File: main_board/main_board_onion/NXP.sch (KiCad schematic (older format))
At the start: 16 parts

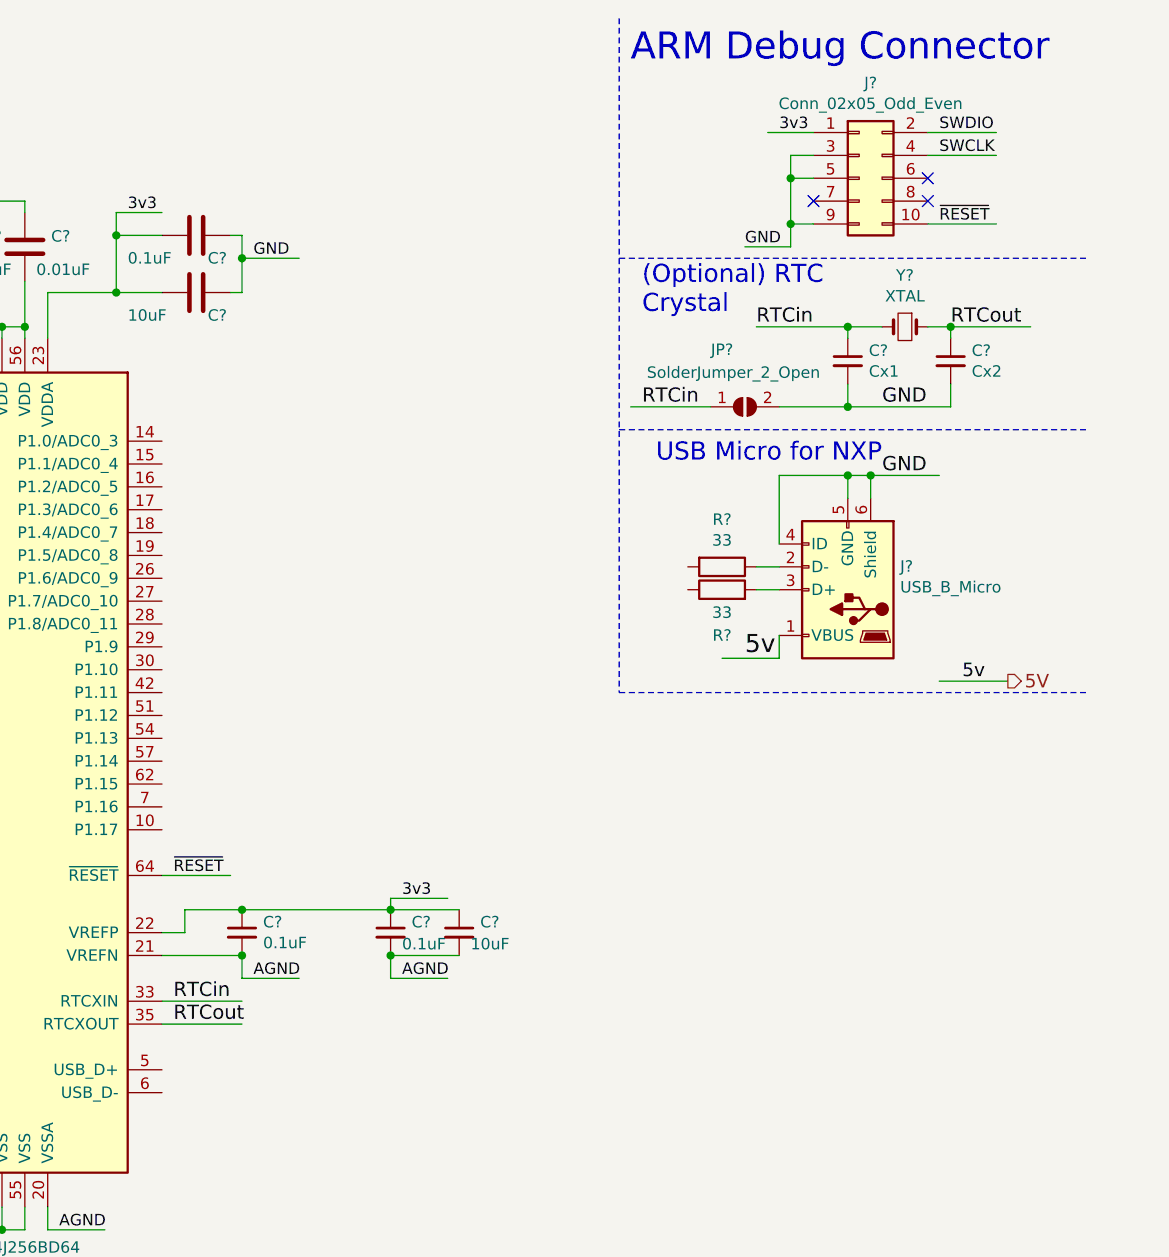
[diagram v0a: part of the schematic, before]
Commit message: Added USB support. Minor additions to Omega board.
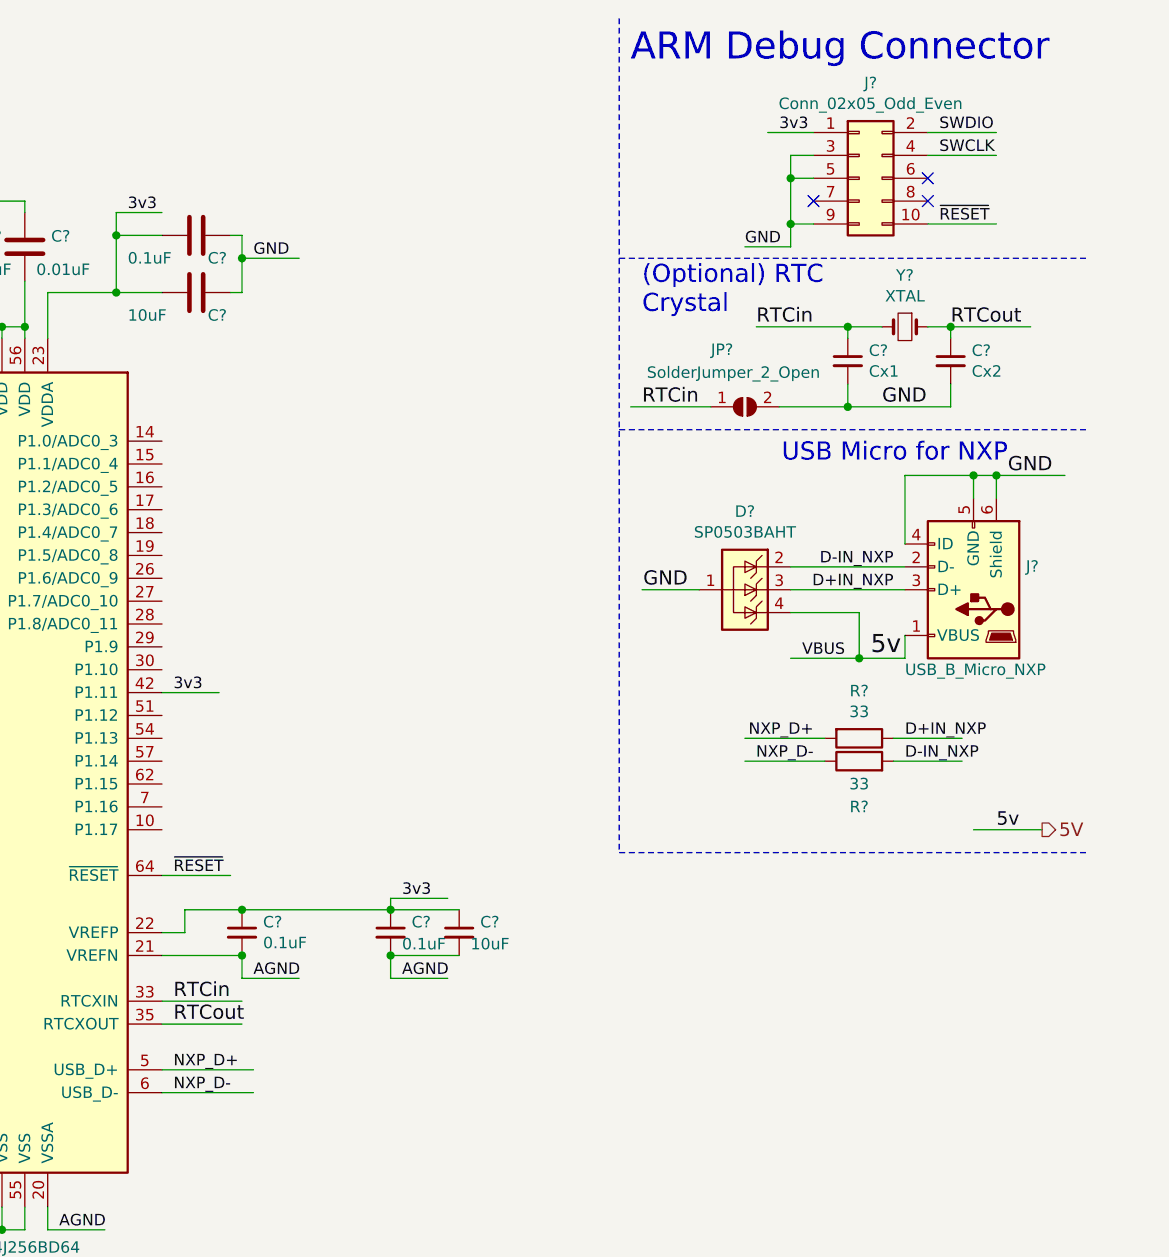
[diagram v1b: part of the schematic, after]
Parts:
- added D?: SP0503BAHT, Package_TO_SOT_SMD:SOT-143, symbol Power_Protection:SP0503BAHT
- J?: value USB_B_Micro -> USB_B_Micro_NXP; footprint (none) -> Connector_USB:USB_Micro-B_Molex-105017-0001
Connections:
- net labels added: D+IN_NXP, D-IN_NXP, NXP_D+, NXP_D-, VBUS
- wire segments 89 -> 100
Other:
- moved on the sheet: J?, R?
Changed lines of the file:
@@
 EESchema Schematic File Version 4
+LIBS:main_board_onion-cache
 EELAYER 26 0
 EELAYER END
 $Descr A4 11693 8268
 encoding utf-8
-Sheet 2 2
+Sheet 2 3
 Title ""
 Date ""
@@
 L Connector:USB_B_Micro J?
 U 1 1 5B63D16B
-P 10150 3000
-F 0 "J?" H 9921 2898 50  0000 R CNN
-F 1 "USB_B_Micro" H 9921 2989 50  0000 R CNN
-F 2 "" H 10300 2950 50  0001 C CNN
-F 3 "~" H 10300 2950 50  0001 C CNN
-	1    10150 3000
+P 10700 3000
+F 0 "J?" H 10471 2898 50  0000 R CNN
+F 1 "USB_B_Micro_NXP" H 11000 3350 50  0000 R CNN
+F 2 "Connector_USB:USB_Micro-B_Molex-105017-0001" H 10850 2950 50  0001 C CNN
+F 3 "~" H 10850 2950 50  0001 C CNN
+	1    10700 3000
 	-1   0    0    1
 $EndComp
 Wire Wire Line
-	10150 2600 10150 2500
-Wire Wire Line
-	10150 2500 10250 2500
-Wire Wire Line
-	10250 2600 10250 2500
-Connection ~ 10250 2500
-Wire Wire Line
-	10250 2500 10550 2500
-Text Label 10300 2500 0    62   ~ 0
-GND
-Wire Wire Line
-	9850 2800 9850 2500
-Wire Wire Line
-	9850 2500 10150 2500
-Connection ~ 10150 2500
+	10700 2600 10700 2500
+Wire Wire Line
+	10700 2500 10800 2500
+Wire Wire Line
+	10800 2600 10800 2500
+Connection ~ 10800 2500
+Wire Wire Line
+	10800 2500 11100 2500
+Text Label 10850 2500 0    62   ~ 0
+GND
+Wire Wire Line
+	10400 2800 10400 2500
+Wire Wire Line
+	10400 2500 10700 2500
+Connection ~ 10700 2500
 $Comp
 L Device:R R?
 U 1 1 5B641EBA
-P 9600 2900
-F 0 "R?" V 9393 2900 50  0000 C CNN
-F 1 "33" V 9484 2900 50  0000 C CNN
-F 2 "" V 9530 2900 50  0001 C CNN
-F 3 "~" H 9600 2900 50  0001 C CNN
-	1    9600 2900
+P 10200 3650
+F 0 "R?" V 9993 3650 50  0000 C CNN
+F 1 "33" V 10084 3650 50  0000 C CNN
+F 2 "" V 10130 3650 50  0001 C CNN
+F 3 "~" H 10200 3650 50  0001 C CNN
+	1    10200 3650
 	0    1    1    0
 $EndComp
@@
 L Device:R R?
 U 1 1 5B641F67
-P 9600 3000
-F 0 "R?" V 9400 3000 50  0000 C CNN
-F 1 "33" V 9500 3000 50  0000 C CNN
-F 2 "" V 9530 3000 50  0001 C CNN
-F 3 "~" H 9600 3000 50  0001 C CNN
-	1    9600 3000
+P 10200 3750
+F 0 "R?" V 10000 3750 50  0000 C CNN
+F 1 "33" V 10100 3750 50  0000 C CNN
+F 2 "" V 10130 3750 50  0001 C CNN
+F 3 "~" H 10200 3750 50  0001 C CNN
+	1    10200 3750
 	0    -1   -1   0
 $EndComp
 Wire Wire Line
-	9850 2900 9750 2900
-Wire Wire Line
-	9850 3000 9750 3000
-Wire Wire Line
-	9850 3200 9850 3300
-Wire Wire Line
-	9850 3300 9600 3300
-Text Label 9700 3300 0    79   ~ 0
+	10400 3200 10400 3300
+Text Label 10250 3300 0    79   ~ 0
 5v
-Text HLabel 10850 3400 2    59   Output ~ 0
+Text HLabel 11000 4050 2    59   Output ~ 0
 5V
 Wire Wire Line
-	10850 3400 10550 3400
-Text Label 10750 3400 2    59   ~ 0
+	11000 4050 10700 4050
+Text Label 10900 4050 2    59   ~ 0
 5v
-Text Notes 10300 2450 2    79   ~ 0
+Text Notes 10850 2450 2    79   ~ 0
 USB Micro for NXP
 Wire Notes Line
-	9150 3450 11200 3450
+	9150 500  9150 4150
+Wire Wire Line
+	10050 3650 9700 3650
+Wire Wire Line
+	10050 3750 9700 3750
+Wire Wire Line
+	7150 3450 7400 3450
+Wire Wire Line
+	9900 3300 10200 3300
+Text Label 9950 3300 0    50   ~ 0
+VBUS
+Wire Wire Line
+	7150 5100 7550 5100
+Text Label 7200 5100 0    50   ~ 0
+NXP_D+
+Text Label 7200 5200 0    50   ~ 0
+NXP_D-
+Wire Wire Line
+	7150 5200 7550 5200
+Text Label 10000 3750 2    50   ~ 0
+NXP_D-
+Text Label 10000 3650 2    50   ~ 0
+NXP_D+
+Text Label 7200 3450 0    50   ~ 0
+3v3
+$Comp
+L Power_Protection:SP0503BAHT D?
+U 1 1 5B678F4C
+P 9700 3000
+F 0 "D?" V 9358 3000 50  0000 C CNN
+F 1 "SP0503BAHT" V 9449 3000 50  0000 C CNN
+F 2 "Package_TO_SOT_SMD:SOT-143" H 9925 2950 50  0001 L CNN
+F 3 "http://www.littelfuse.com/~/media/files/littelfuse/technical%20resources/documents/data%20sheets/sp05xxba.pdf" H 9825 3125 50  0001 C CNN
+	1    9700 3000
+	0    1    1    0
+$EndComp
+Wire Wire Line
+	10350 3650 10650 3650
+Wire Wire Line
+	10350 3750 10650 3750
+Wire Wire Line
+	9900 2900 10400 2900
+Wire Wire Line
+	9900 3000 10400 3000
+Wire Wire Line
+	9900 3100 10200 3100
+Wire Wire Line
+	10200 3100 10200 3300
+Connection ~ 10200 3300
+Wire Wire Line
+	10200 3300 10400 3300
+Text Label 10350 3000 2    50   ~ 0
+D+IN_NXP
+Text Label 10350 2900 2    50   ~ 0
+D-IN_NXP
+Text Label 10400 3650 0    50   ~ 0
+D+IN_NXP
+Text Label 10400 3750 0    50   ~ 0
+D-IN_NXP
+Text Label 9450 3000 2    62   ~ 0
+GND
+Wire Wire Line
+	9500 3000 9250 3000
 Wire Notes Line
-	9150 500  9150 3450
+	9150 4150 11200 4150
 $EndSCHEMATC

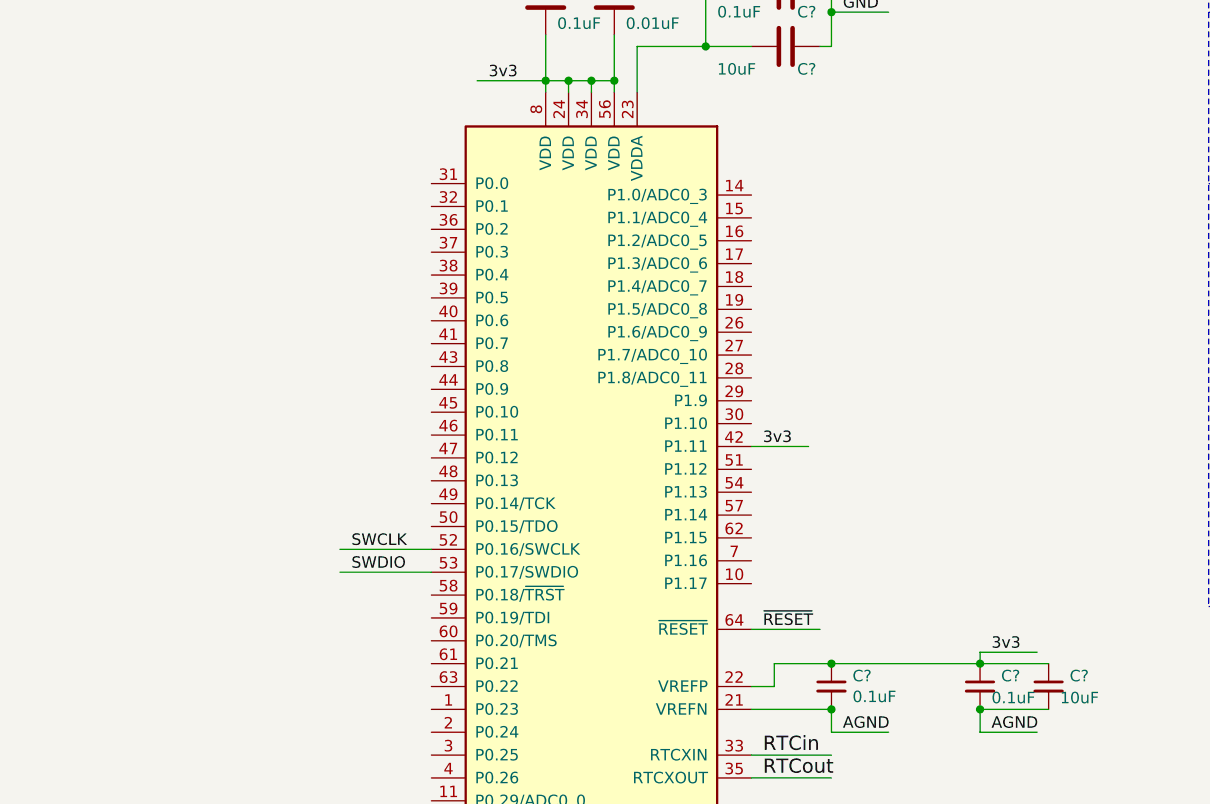
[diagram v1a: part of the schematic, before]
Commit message: Added 24V power, communication between Omega and NXP and Finished ethernet
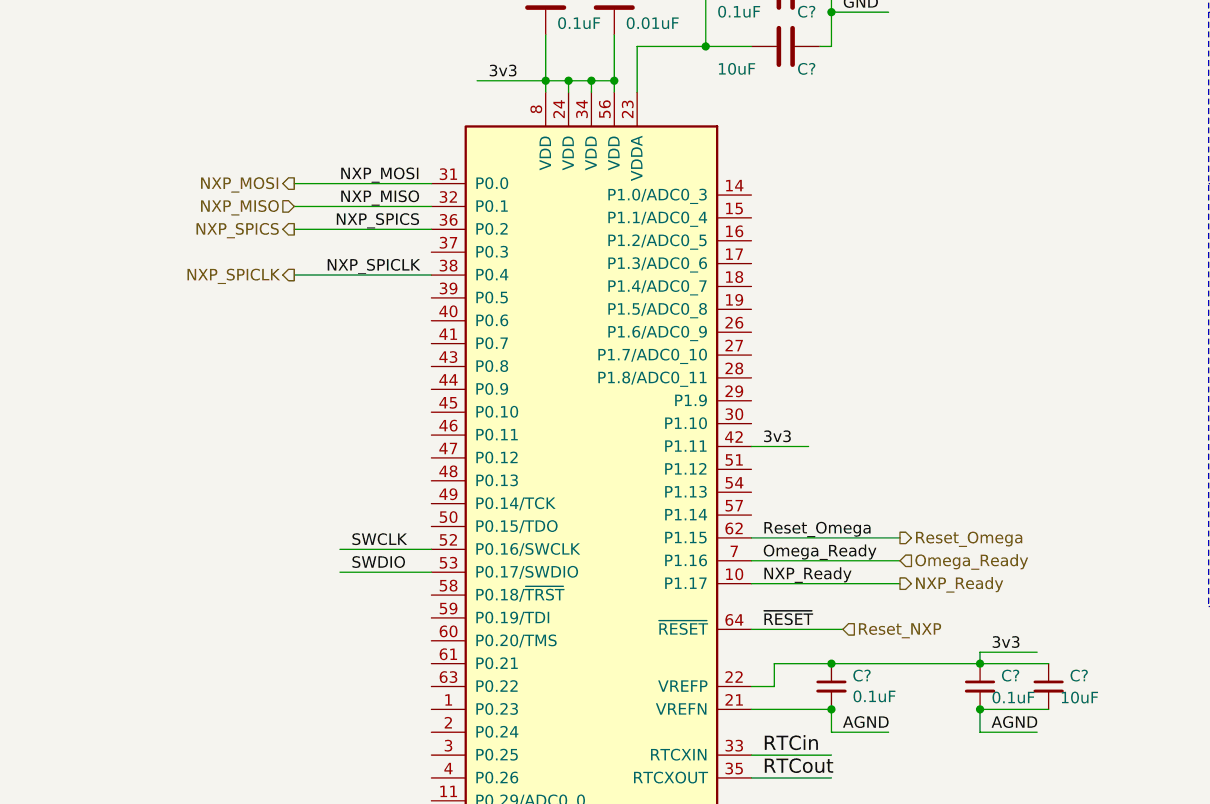
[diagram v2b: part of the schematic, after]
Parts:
- JP?: footprint (none) -> Resistor_SMD:R_0805_2012Metric
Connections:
- net labels added: NXP_MISO, NXP_MOSI, NXP_Ready, NXP_SPICLK, NXP_SPICS, Omega_Ready, Reset_NXP, Reset_Omega
- wire segments 100 -> 107
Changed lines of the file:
@@
 SWDIO
 Wire Wire Line
-	7150 4250 7450 4250
+	7150 4250 7550 4250
 Text Label 7200 4250 0    50   ~ 0
 ~RESET
@@
 F 0 "JP?" H 9600 2450 50  0000 C CNN
 F 1 "SolderJumper_2_Open" H 9650 2350 50  0000 C CNN
-F 2 "" H 9700 2200 50  0001 C CNN
+F 2 "Resistor_SMD:R_0805_2012Metric" H 9700 2200 50  0001 C CNN
 F 3 "~" H 9700 2200 50  0001 C CNN
 	1    9700 2200
@@
 Wire Notes Line
 	9150 4150 11200 4150
+Text Label 5700 2300 2    50   ~ 0
+NXP_MOSI
+Text Label 5700 2400 2    50   ~ 0
+NXP_MISO
+Text Label 5700 2500 2    50   ~ 0
+NXP_SPICS
+Text Label 5700 2700 2    50   ~ 0
+NXP_SPICLK
+Wire Wire Line
+	5750 2700 5150 2700
+Wire Wire Line
+	5750 2500 5150 2500
+Wire Wire Line
+	5750 2400 5150 2400
+Wire Wire Line
+	5750 2300 5150 2300
+Text Label 7200 4050 0    50   ~ 0
+NXP_Ready
+Wire Wire Line
+	7150 4050 7800 4050
+Text Label 7200 3950 0    50   ~ 0
+Omega_Ready
+Wire Wire Line
+	7150 3950 7800 3950
+Text HLabel 7800 4050 2    50   Output ~ 0
+NXP_Ready
+Text HLabel 7800 3950 2    50   Input ~ 0
+Omega_Ready
+Text HLabel 7550 4250 2    50   Input ~ 0
+Reset_NXP
+Text HLabel 5150 2300 0    50   Output ~ 0
+NXP_MOSI
+Text HLabel 5150 2400 0    50   Input ~ 0
+NXP_MISO
+Text HLabel 5150 2500 0    50   Output ~ 0
+NXP_SPICS
+Text HLabel 5150 2700 0    50   Output ~ 0
+NXP_SPICLK
+Text Label 7200 3850 0    50   ~ 0
+Reset_Omega
+Wire Wire Line
+	7150 3850 7800 3850
+Text HLabel 7800 3850 2    50   Output ~ 0
+Reset_Omega
 $EndSCHEMATC
